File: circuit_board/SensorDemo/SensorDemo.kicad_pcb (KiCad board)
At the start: 4 copper layers, 46 x 68 mm, 59 parts, among them K1 PB_SMD, P1 CONN3X2, P2 CONN3X2, U1 TLV1117-33CDCYR, U2 dsPIC33EP32GP502, U3 LTC1658, U4 INA126, U5 REF1925, U6 REF1925, X1 8MHz

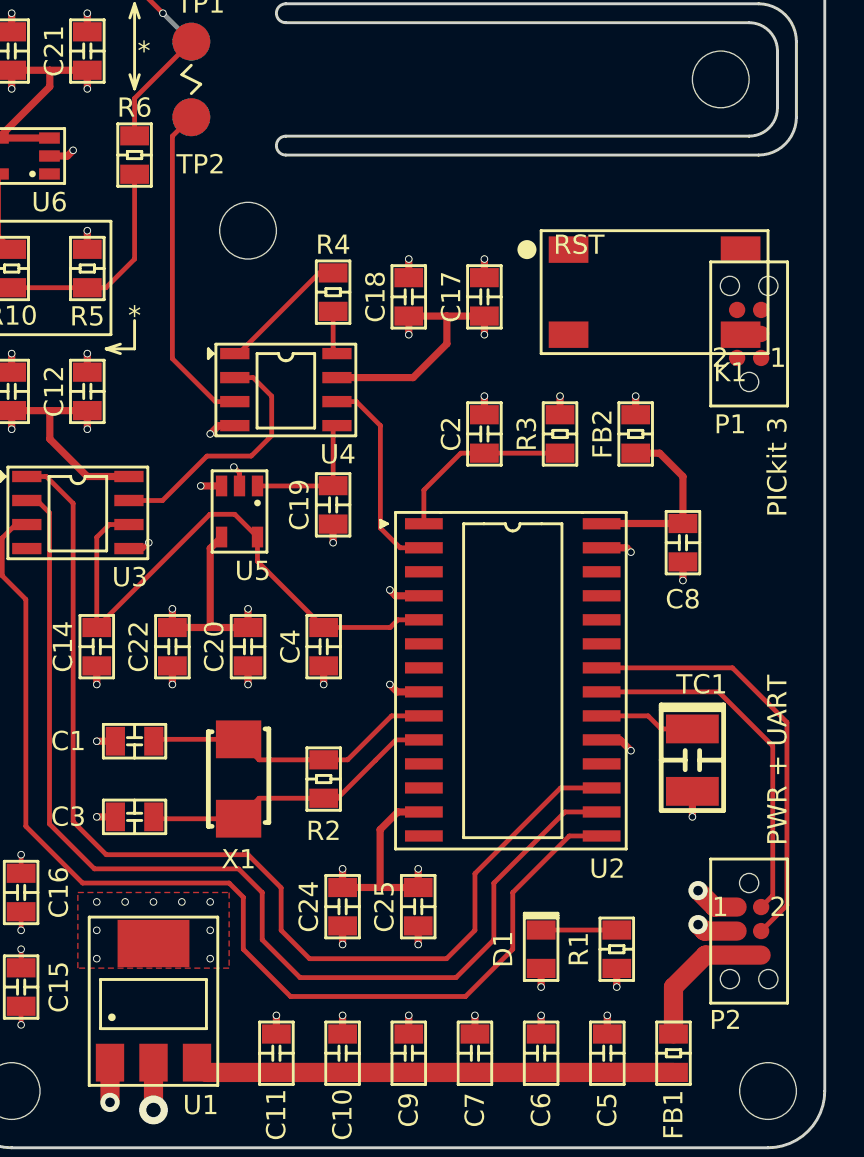
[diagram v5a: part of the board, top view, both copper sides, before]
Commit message: updated SensoDemo and ProgramBoard
INA126 is replaced by INA333.
TC2050-IDC-NL cable will be used for powering and programming.
both boards should be done.
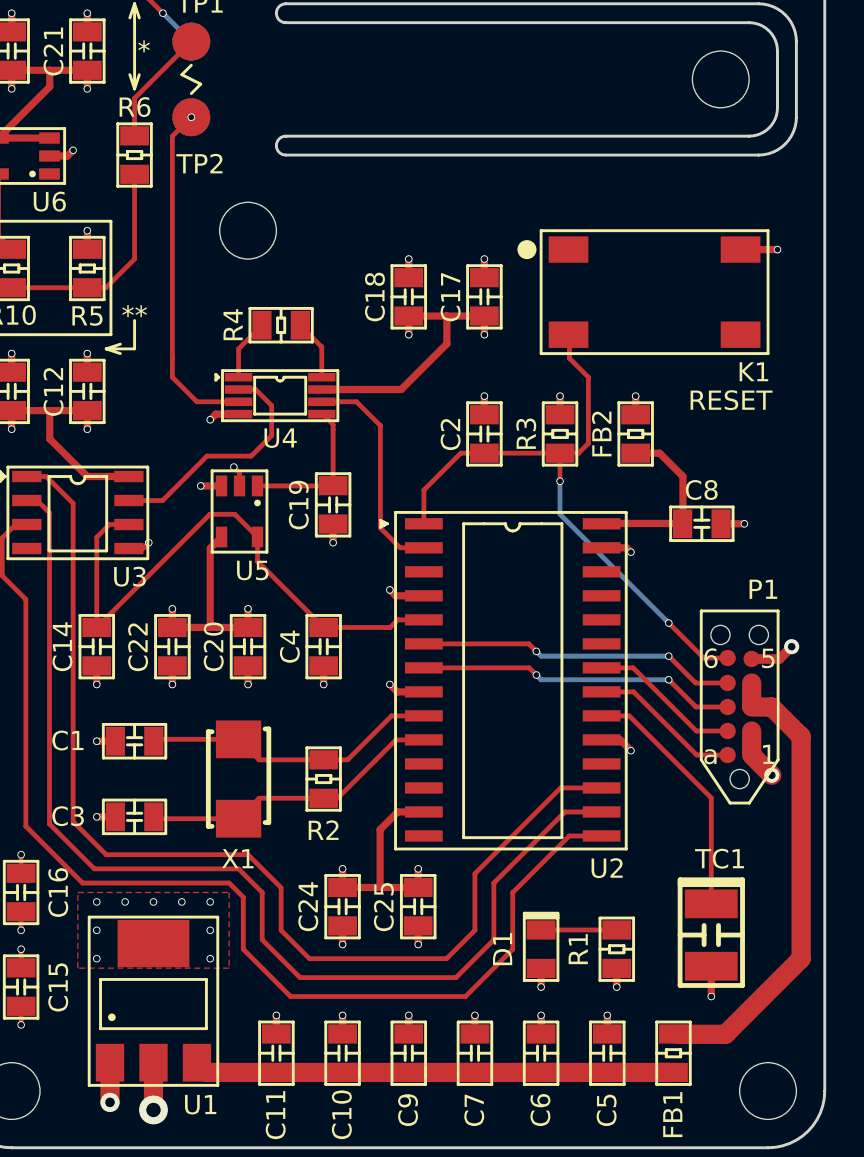
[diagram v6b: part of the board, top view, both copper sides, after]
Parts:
- removed P2: CONN3X2, SensorDemo_pcb:TC2030
- P1: value CONN3X2 -> TC2050_IDC_NL; footprint SensorDemo_pcb:TC2030 -> SensorDemo_pcb:TC2050
- U4: value INA126 -> INA333; footprint SensorDemo_pcb:SOIC-8 -> SensorDemo_pcb:MSOP-8
- moved P1 21.0 mm to (159.0, 105.5)
- moved TC1 9.30 mm to (157.5, 113.8)
- moved R4 3.26 mm to (134.8, 81.5), turned to 0 degrees
- moved U4 2.80 mm to (132.5, 84.2)
- moved C8 1.41 mm to (157.0, 92.0), turned to 0 degrees
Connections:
- FB1 pad 1: Net-(FB1-Pad1) -> +5V
- P1 pad 1: /~MCLR -> GND
- P1 pad 2: +3V3 -> GND
- P1 pad 3: GND -> +5V
- P1 pad 4: /PGD -> +5V
- P1 pad 5: /PGC -> +3V3
- P1 pad 6: (no net) -> /~MCLR
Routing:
- net +5V: track 0.00 -> 24.4 mm
- net /~MCLR: track 9.79 -> 32.9 mm, vias 0 -> 2
- net /PGC: track 0.00 -> 16.9 mm, vias 0 -> 2
- net /PGD: track 0.00 -> 16.9 mm, vias 0 -> 2
- net /ucRX: track 22.6 -> 8.05 mm
- net /ucTX: track 19.0 -> 8.05 mm
- net Net-(FB1-Pad1): track 7.82 -> 0.00 mm
- net Net-(TC1-Pad1): track 5.09 -> 12.8 mm
- net Net-(R4-Pad1): track 6.77 -> 3.27 mm
- net +3V3: track 72.9 -> 76.4 mm, vias 27 -> 28
- net Net-(R4-Pad2): track 2.34 -> 3.23 mm
- net /Vsen: track 17.4 -> 18.2 mm, vias 0 -> 1
- net /sensVal: track 11.0 -> 11.8 mm
- net Net-(U3-Pad7): track 13.4 -> 12.7 mm
- net /Vbias: track 7.26 -> 7.95 mm
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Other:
- net class 3V3: clearance 0.254 -> 0.1524
- net class Default: clearance 0.254 -> 0.1524
- net class GND: clearance 0.254 -> 0.1524
- rule trace_clearance: 0.254 -> 0.1524
- board text added: "* Sensor series resistor R6: TP1 & TP2 R9: TP3 & TP4 ** Sensor bias selection R5: LDO 3.3V R10: REF19xx"
- board text added: "**"
- board text added: "RESET"
- board text removed: "* R5: LDO 3.3V R10: REF19xx"
- board text removed: "1 GND 2 TX 3 GND 4 RX 5 VCC 6 VCC"
- board text removed: "1 ~MCLR 2 VDD 3 GND 4 PGD 5 PGC 6 N.C."
- board text removed: "PICkit 3"
- board text removed: "PWR + UART"
- board text removed: "RST"

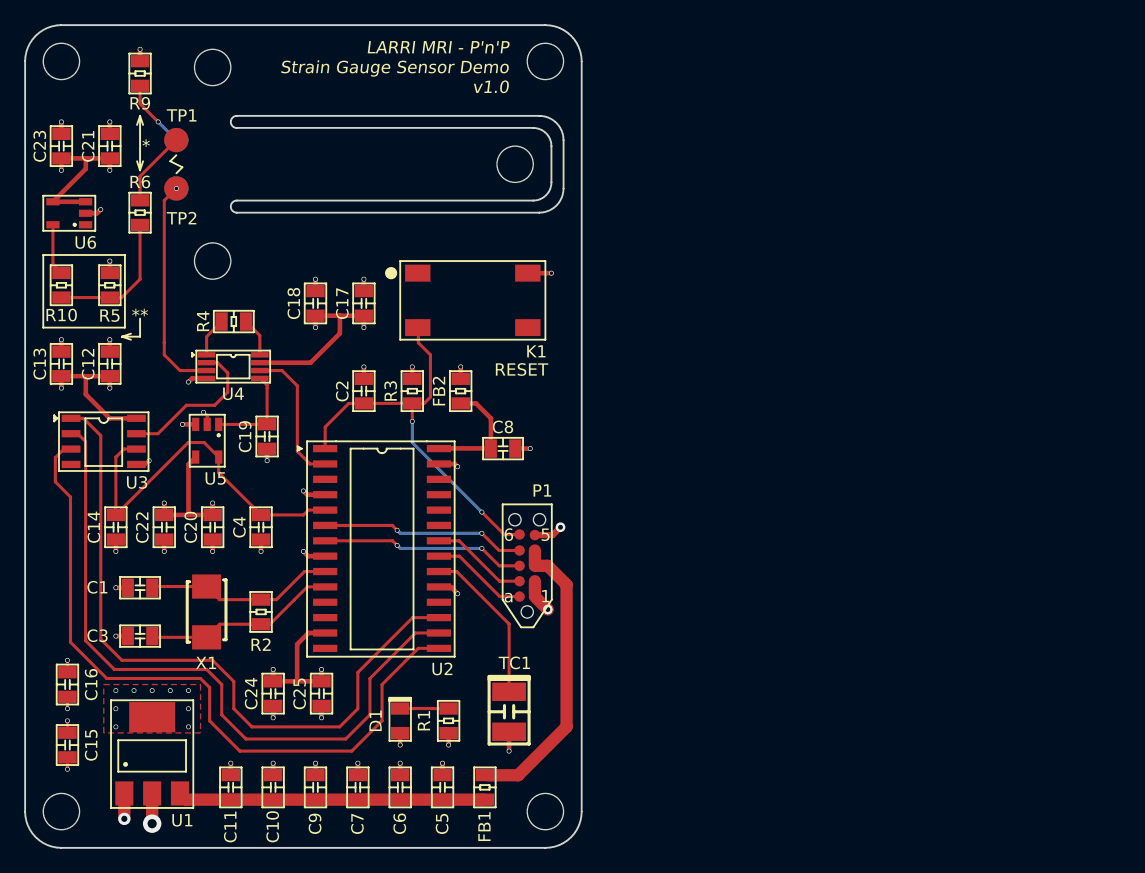
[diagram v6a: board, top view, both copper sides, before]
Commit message: testing pins added
updated PCB design:
added testing pins on the SensorDemo.
ProgramBoard modified GND connections.
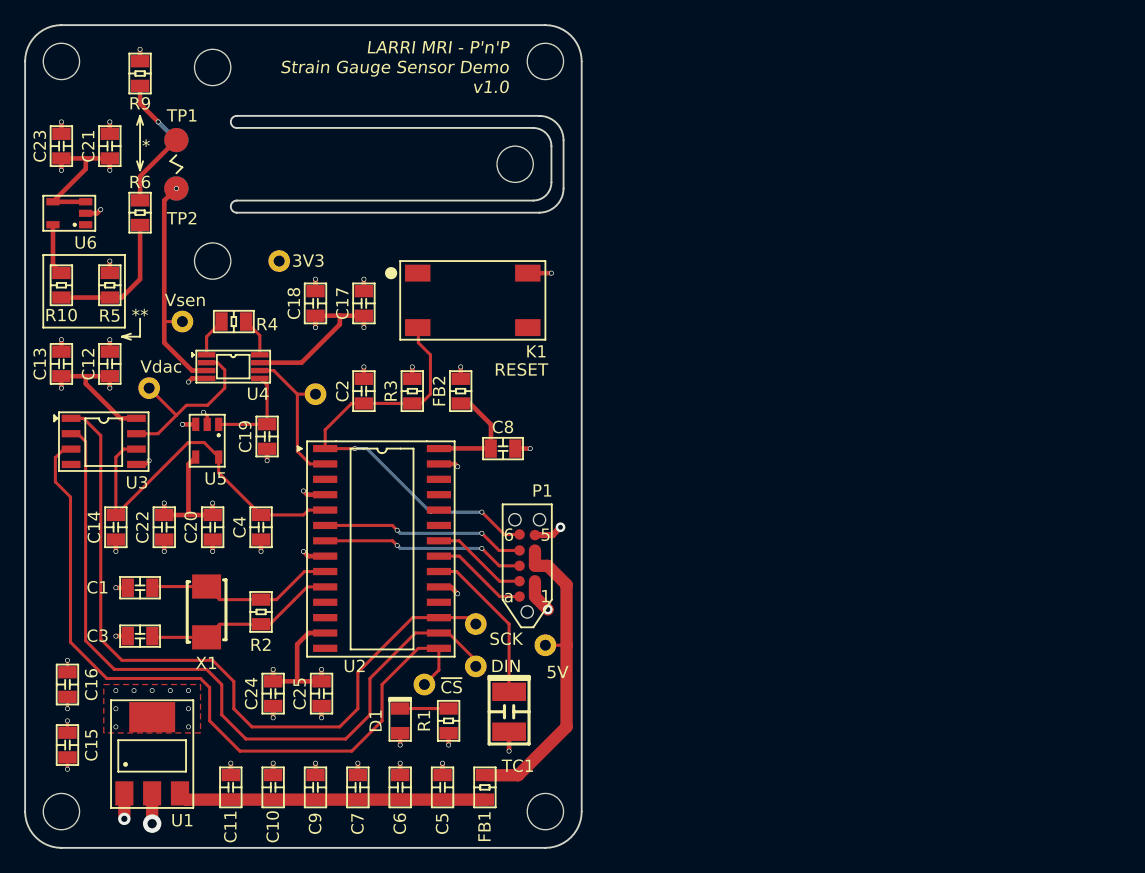
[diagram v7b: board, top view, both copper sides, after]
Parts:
- added 3V3: TP_TH, SensorDemo_pcb:TP_TH, F.Cu at (138.5, 76.5)
- added 5V: TP_TH, SensorDemo_pcb:TP_TH, F.Cu at (160.5, 108.2)
- added DIN: TP_TH, SensorDemo_pcb:TP_TH, F.Cu at (154.8, 110.0)
- added SCK: TP_TH, SensorDemo_pcb:TP_TH, F.Cu at (154.8, 106.5)
- added Vdac: TP_TH, SensorDemo_pcb:TP_TH, F.Cu at (127.8, 87.0)
- added Vsen: TP_TH, SensorDemo_pcb:TP_TH, F.Cu at (130.5, 81.5)
- added sensVal: TP_TH, SensorDemo_pcb:TP_TH, F.Cu at (141.5, 87.5)
- added ~CS: TP_TH, SensorDemo_pcb:TP_TH, F.Cu at (150.5, 111.5)
- moved G*** 5.01 mm to (128.0, 122.2)
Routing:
- net Net-(U2-Pad16): track 57.3 -> 61.8 mm
- net Net-(U2-Pad15): track 58.4 -> 61.9 mm
- net Net-(U2-Pad17): track 57.6 -> 60.9 mm
- net /~MCLR: track 32.9 -> 35.9 mm
- net Net-(U3-Pad7): track 12.7 -> 15.3 mm
- net +5V: track 24.4 -> 26.1 mm
- net /sensVal: track 11.8 -> 12.9 mm
- net +3V3: track 76.4 -> 75.4 mm
- net /Vsen: track 18.2 -> 19.1 mm
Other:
- board text added: "Daniel &"
- board text removed: "Daniel & Ruoshi"

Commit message: modified according to Doug
on SensorDemo, fiducial marks are added, via size changed to .25mm and .55mm, decreased solder mask gap between pins on MSOP8 package.
the minimum JLC can take between pins is .2mm for green mask.
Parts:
- added FD: Val**, SensorDemo_pcb:FD_1MM_C, F.Cu at (119.5, 103.0)
- added FD: Val**, SensorDemo_pcb:FD_1MM_R, F.Cu at (160.5, 89.0)
- added FD: Val**, SensorDemo_pcb:FD_1MM_R, F.Cu at (161.5, 119.0)
- added FD: Val**, SensorDemo_pcb:FD_1MM_C, F.Cu at (158.0, 62.5)
- added FD: Val**, SensorDemo_pcb:FD_1MM_C, F.Cu at (123.0, 119.5)
- added FD: Val**, SensorDemo_pcb:FD_1MM_R, F.Cu at (123.0, 62.5)
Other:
- rule via_min_drill: 0.3 -> 0.25
